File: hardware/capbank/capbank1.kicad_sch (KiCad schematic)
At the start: 8 parts, among them J2 Jack-DC, U5 PAI130M61

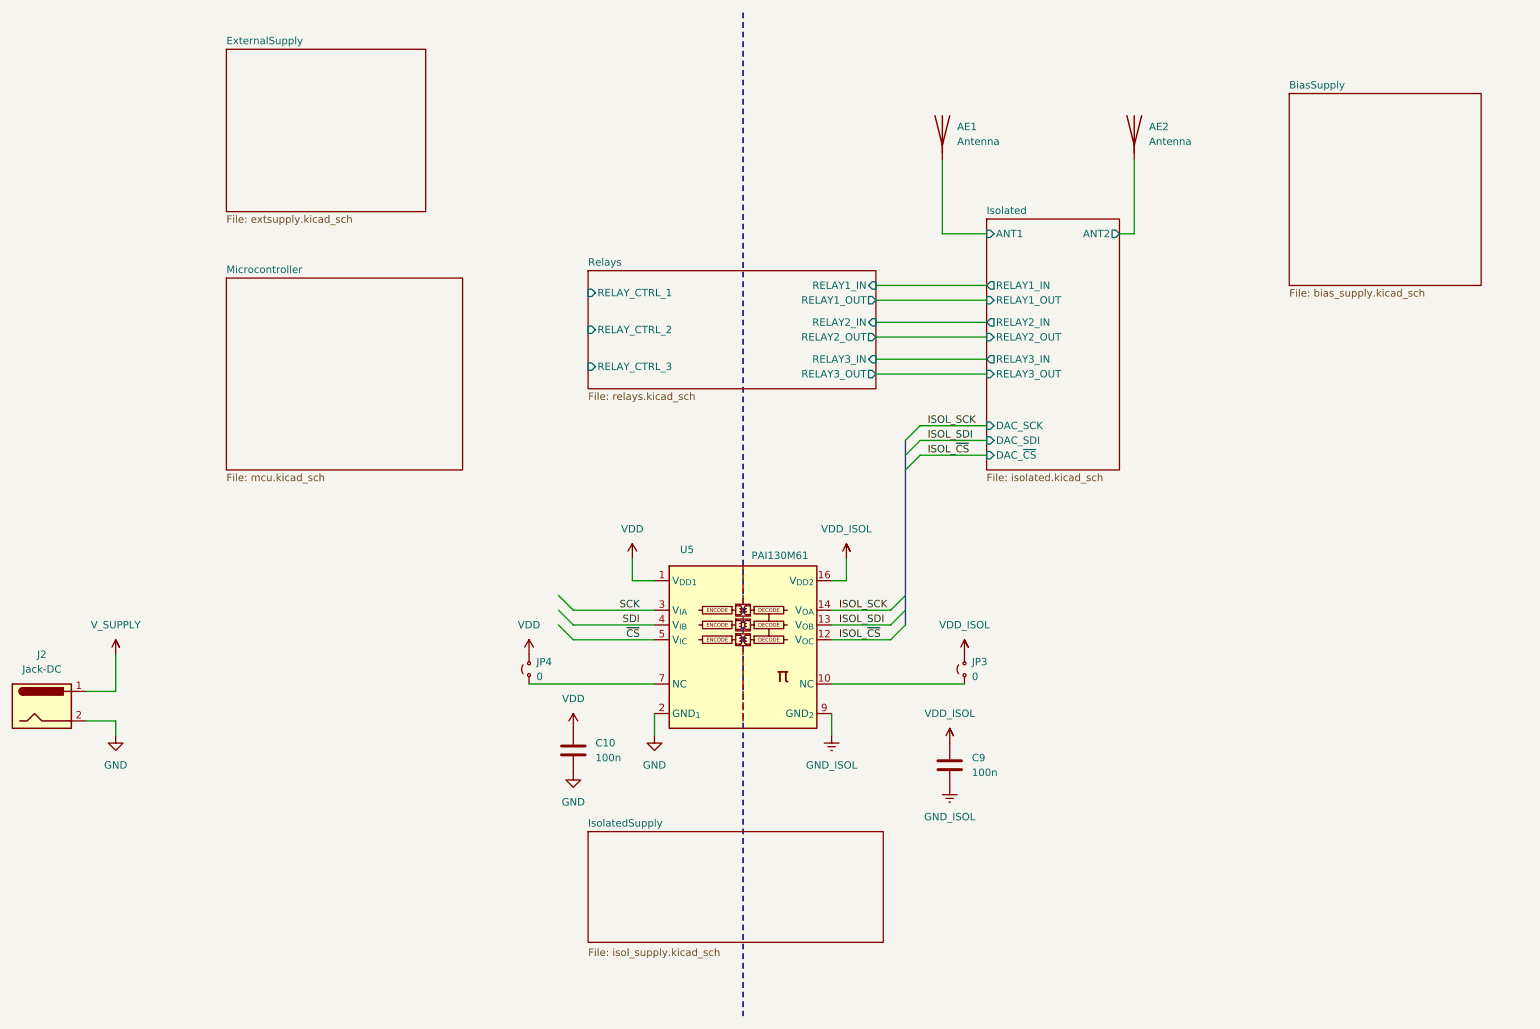
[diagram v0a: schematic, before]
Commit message: Progress, layout nearly completed, build oscillator on breadboard
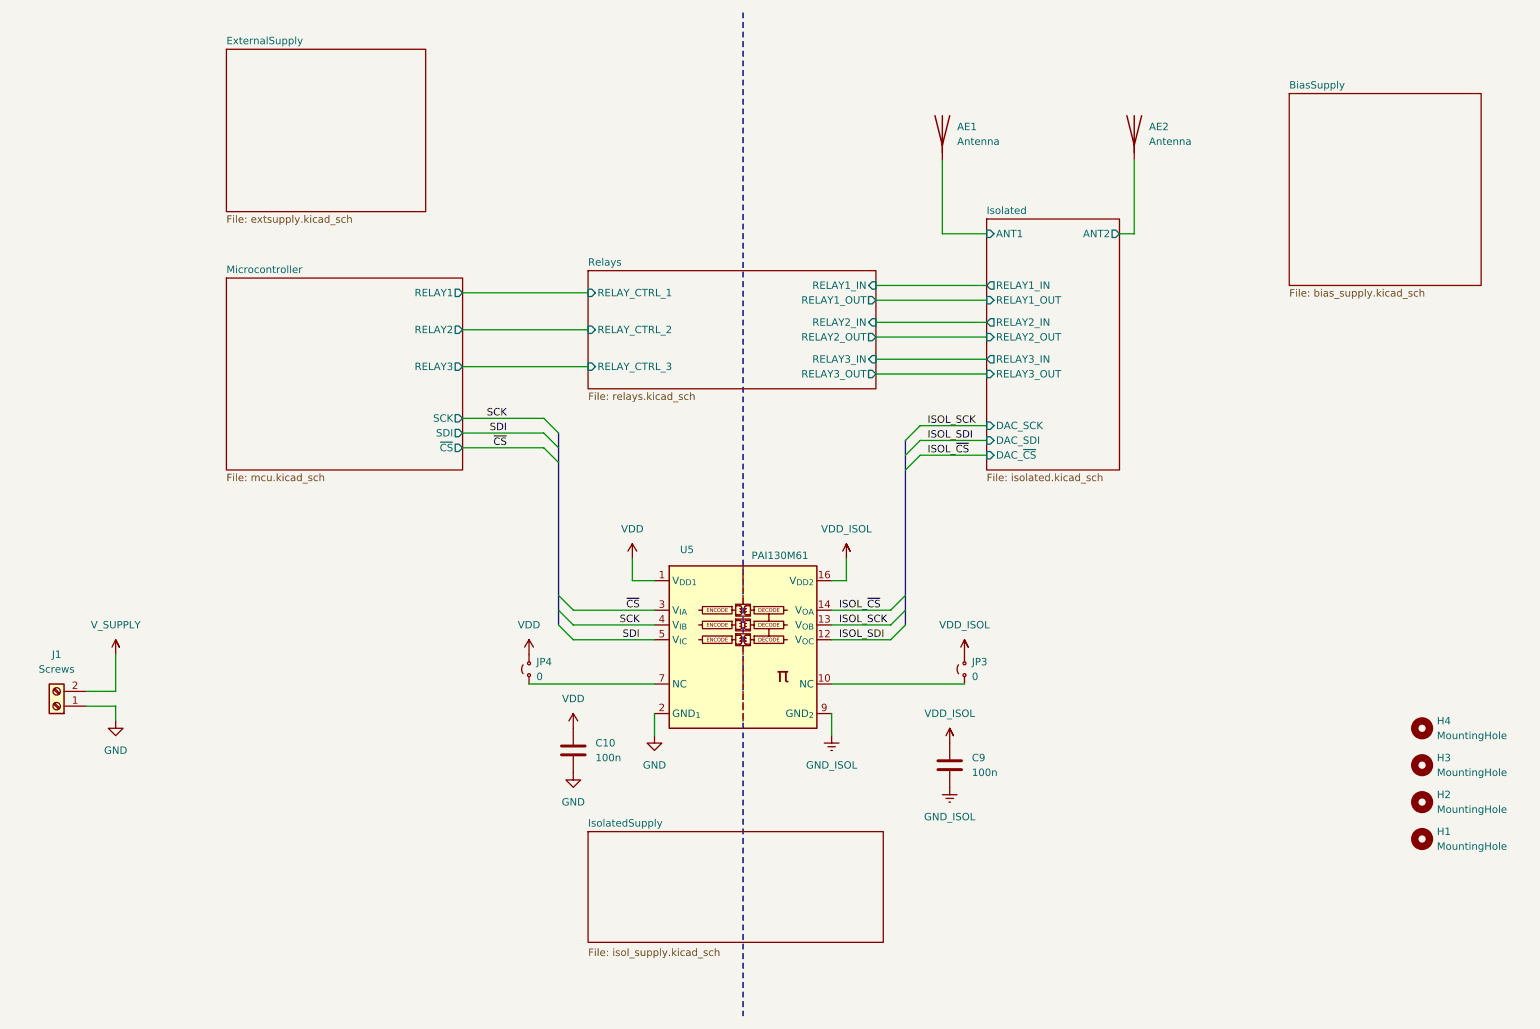
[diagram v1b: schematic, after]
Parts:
- removed J2: Jack-DC, Connector_BarrelJack:BarrelJack_Horizontal, symbol Connector:Jack-DC
- added H1, H2, H3, H4: MountingHole, MountingHole:MountingHole_3.2mm_M3, symbol Mechanical:MountingHole
- added J1: Screws, TerminalBlock_Phoenix:TerminalBlock_Phoenix_MPT-0,5-2-2.54_1x02_P2.54mm_Horizontal, symbol Connector:Screw_Terminal_01x02
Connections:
- net GND: now also J1.1 (Pin_1)
- net ISOL_SCK: now also U5.13 (V_{OB}); no longer U5.14 (V_{OA})
- net ISOL_SDI: now also U5.12 (V_{OC}); no longer U5.13 (V_{OB})
- net ISOL_~{CS}: now also U5.14 (V_{OA}); no longer U5.12 (V_{OC})
- net SCK: now also U5.4 (V_{IB}); no longer U5.3 (V_{IA})
- net SDI: now also U5.5 (V_{IC}); no longer U5.4 (V_{IB})
- net V_SUPPLY: now also J1.2 (Pin_2)
- net ~{CS}: now also U5.3 (V_{IA}); no longer U5.5 (V_{IC})
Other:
- sheet Microcontroller ports: added RELAY1, RELAY2, RELAY3, SCK, SDI, ~{CS}; removed none
